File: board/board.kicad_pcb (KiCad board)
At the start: 2 copper layers, 21 x 13 mm, 1 part

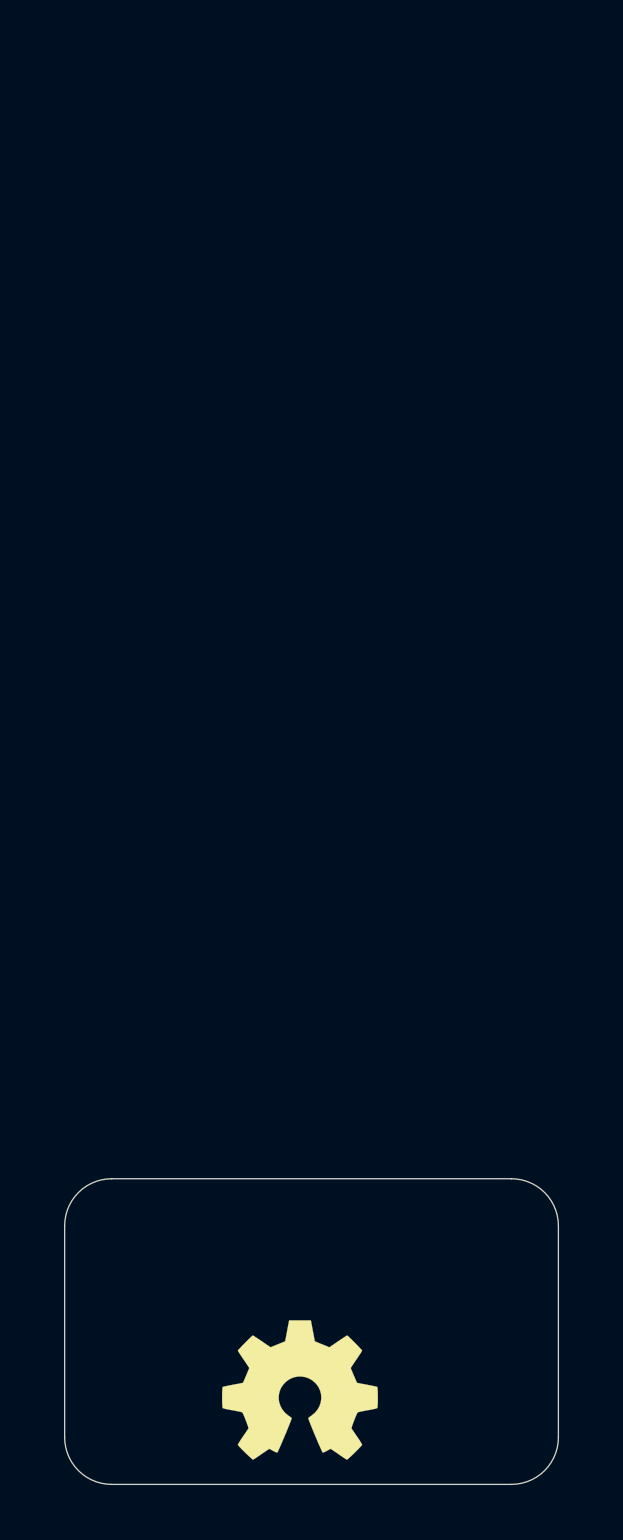
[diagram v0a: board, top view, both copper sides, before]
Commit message: modernized the legacy version
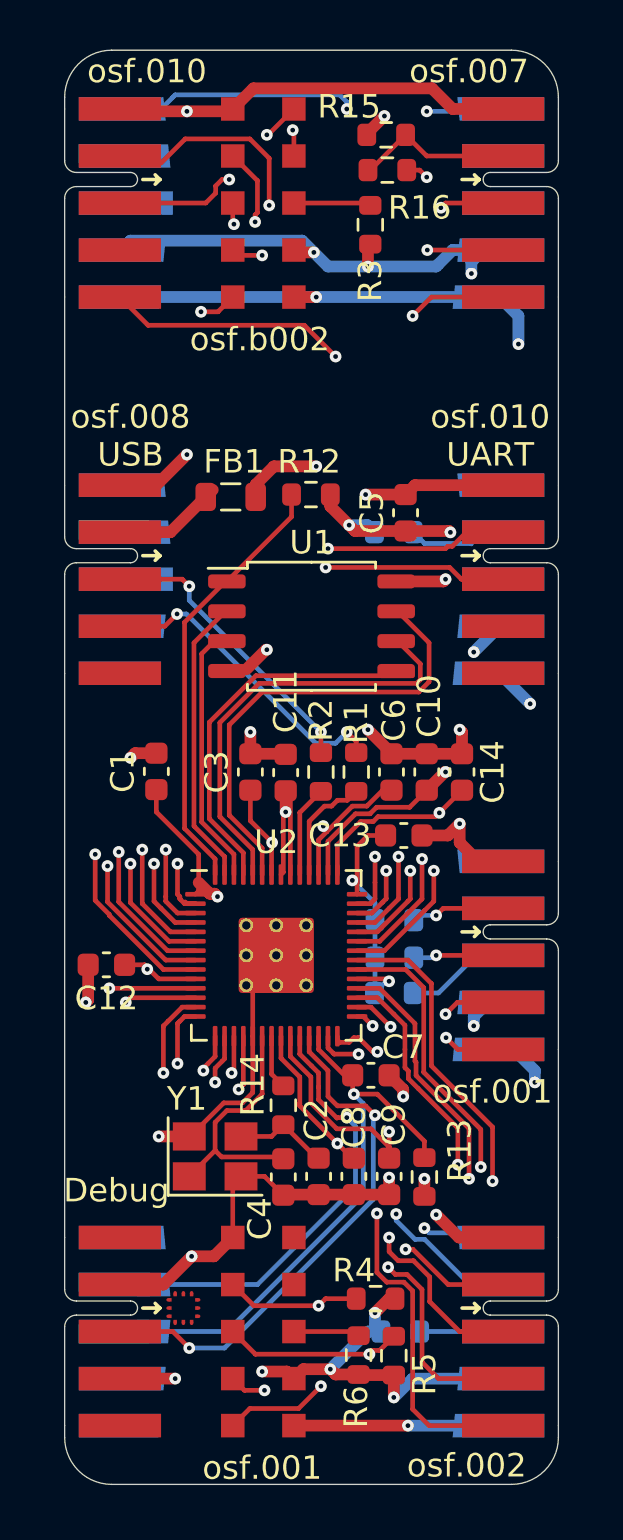
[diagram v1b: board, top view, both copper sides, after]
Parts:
- added C1: 100nF, Capacitor_SMD:C_0603_1608Metric, F.Cu at (143.9, 72.7)
- added C10: 100nF, Capacitor_SMD:C_0603_1608Metric, F.Cu at (155.4, 72.7)
- added C11: 100nF, Capacitor_SMD:C_0603_1608Metric, F.Cu at (149.4, 72.7)
- added C12: 100nF, Capacitor_SMD:C_0603_1608Metric, F.Cu at (141.8, 80.9)
- added C13: 2.2uF, Capacitor_SMD:C_0603_1608Metric, F.Cu at (154.4, 75.4)
- added C14: 2.2uF, Capacitor_SMD:C_0603_1608Metric, F.Cu at (156.9, 72.7)
- added C2: 12pF, Capacitor_SMD:C_0603_1608Metric, F.Cu at (150.8, 89.9)
- added C3: 100nF, Capacitor_SMD:C_0603_1608Metric, F.Cu at (147.9, 72.7)
- added C4: 12pF, Capacitor_SMD:C_0603_1608Metric, F.Cu at (149.3, 89.9)
- added C5: 100nF, Capacitor_SMD:C_0603_1608Metric, F.Cu at (154.5, 61.7)
- added C6: 100nF, Capacitor_SMD:C_0603_1608Metric, F.Cu at (153.9, 72.7)
- added C7: 1nF, Capacitor_SMD:C_0603_1608Metric, F.Cu at (153.0, 85.6)
- added C8: 100nF, Capacitor_SMD:C_0603_1608Metric, F.Cu at (152.3, 89.9)
- added C9: 2.2uF, Capacitor_SMD:C_0603_1608Metric, F.Cu at (153.8, 89.9)
- added FB1: Ferrite_Bead_Small, Inductor_SMD:L_0805_2012Metric, F.Cu at (147.1, 61.0)
- added J1: UART, on_edge:on_edge_2x05_device, F.Cu at (140.0, 48.5)
- added J2: 008_USB, on_edge:on_edge_2x05_device, F.Cu at (140.0, 64.5)
- added J3: DebugEdge_02x05, on_edge:debug_edge_2x05_device, F.Cu at (140.0, 96.5)
- added J4: SPI_2x3, on_edge:on_edge_2x05_up_host, F.Cu at (150.8, 48.5)
- added J5: ADC_2x3, on_edge:on_edge_2x05_host, F.Cu at (161.0, 48.5)
- added J6: I2C_2x2, on_edge:on_edge_2x05_up_host, F.Cu at (150.8, 96.5)
- added J7: SPI_2x3, on_edge:on_edge_2x05_host, F.Cu at (161.0, 96.5)
- added J8: I2C_2x2, on_edge:on_edge_2x05_host, F.Cu at (161.0, 80.5)
- added J9: UART_2x2, on_edge:on_edge_2x05_host, F.Cu at (161.0, 64.5)
- added R1: 27R, Resistor_SMD:R_0603_1608Metric, F.Cu at (152.4, 72.7)
- added R10: 10k, Resistor_SMD:R_0603_1608Metric, B.Cu at (154.0, 82.1)
- added R11: 10k, Resistor_SMD:R_0603_1608Metric, B.Cu at (154.0, 62.5)
- added R12: d.n.p, Resistor_SMD:R_0603_1608Metric, F.Cu at (150.5, 60.9)
- added R13: 10k, Resistor_SMD:R_0603_1608Metric, F.Cu at (155.3, 89.9)
- added R14: 1k, Resistor_SMD:R_0603_1608Metric, F.Cu at (149.3, 86.9)
- added R15: 200R, Resistor_SMD:R_0603_1608Metric, F.Cu at (153.7, 45.6)
- added R16: 1R, Resistor_SMD:R_0603_1608Metric, F.Cu at (153.7, 47.1)
- added R2: 27R, Resistor_SMD:R_0603_1608Metric, F.Cu at (150.9, 72.7)
- added R3: 10k, Resistor_SMD:R_0603_1608Metric, F.Cu at (153.0, 49.4)
- added R4: 2k, Resistor_SMD:R_0603_1608Metric, F.Cu at (153.2, 95.1)
- added R5: 2k, Resistor_SMD:R_0603_1608Metric, F.Cu at (154.0, 97.5)
- added R6: 10k, Resistor_SMD:R_0603_1608Metric, F.Cu at (152.5, 97.5)
- added R7: 2k, Resistor_SMD:R_0603_1608Metric, B.Cu at (154.0, 79.0)
- added R8: 2k, Resistor_SMD:R_0603_1608Metric, B.Cu at (154.0, 80.6)
- added R9: 10k, Resistor_SMD:R_0603_1608Metric, B.Cu at (154.3, 96.5)
- added U1: W25Q128JVS, Package_SO:SOIC-8_5.23x5.23mm_P1.27mm, F.Cu at (150.5, 66.5)
- added U2: RP2040, b018:RP2040-QFN-56, F.Cu at (149.0, 80.5)
- added Y1: 12MhZ, Crystal:Crystal_SMD_Abracon_ABM8G-4Pin_3.2x2.5mm, F.Cu at (146.4, 89.0)
- LOGO1: moved to B.Cu
- moved LOGO1 42.8 mm to (151.3, 56.2), turned to 180 degrees
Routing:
- net +3V3: track 0.00 -> 199.4 mm, vias 0 -> 22
- net GND: track 0.00 -> 166.7 mm, vias 0 -> 15
- net +5V: track 0.00 -> 95.8 mm, vias 0 -> 6
- net /GPIO25: track 0.00 -> 52.5 mm, vias 0 -> 2
- net /GPIO7: track 0.00 -> 45.7 mm, vias 0 -> 2
- net /GPIO24: track 0.00 -> 42.8 mm, vias 0 -> 2
- net /~{SPI0_CS}: track 0.00 -> 42.4 mm, vias 0 -> 2
- net /UART0_TX: track 0.00 -> 41.8 mm, vias 0 -> 2
- net /UART0_RX: track 0.00 -> 41.5 mm, vias 0 -> 2
- net /ADC3: track 0.00 -> 38.5 mm, vias 0 -> 2
- net /SPI0_TX: track 0.00 -> 37.8 mm, vias 0 -> 2
- net Net-(C14-Pad1): track 0.00 -> 36.8 mm, vias 0 -> 2
- net Net-(C3-Pad1): track 0.00 -> 36.6 mm, vias 0 -> 3
- net /SPI0_RX: track 0.00 -> 36.1 mm, vias 0 -> 2
- net /ADC0: track 0.00 -> 35.5 mm, vias 0 -> 2
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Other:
- board size 21 x 13 mm -> 21 x 61 mm
- copper layers 2 -> 4
- board text added: "Debug"
- board text added: "osf.001"
- board text added: "osf.002"
- board text added: "osf.007"
- board text added: "osf.008 USB"
- board text added: "osf.010"
- board text added: "osf.010 UART"
- board text added: "osf.b002"
